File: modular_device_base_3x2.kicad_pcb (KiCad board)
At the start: 2 copper layers, 83.8 x 40.6 mm, 34 parts, among them P1 PWR_JACK_2.5x5.5, P2 BNC_DOUBLE_RA, P3 HEADER_01X03_SMD_RA, P4 HEADER_01X02_SMD_RA, P5 HEADER_01X03_SMD_RA, P6 HEADER_01X02_SMD_RA, SW1 KT_SWITCH, U1 MAX6817

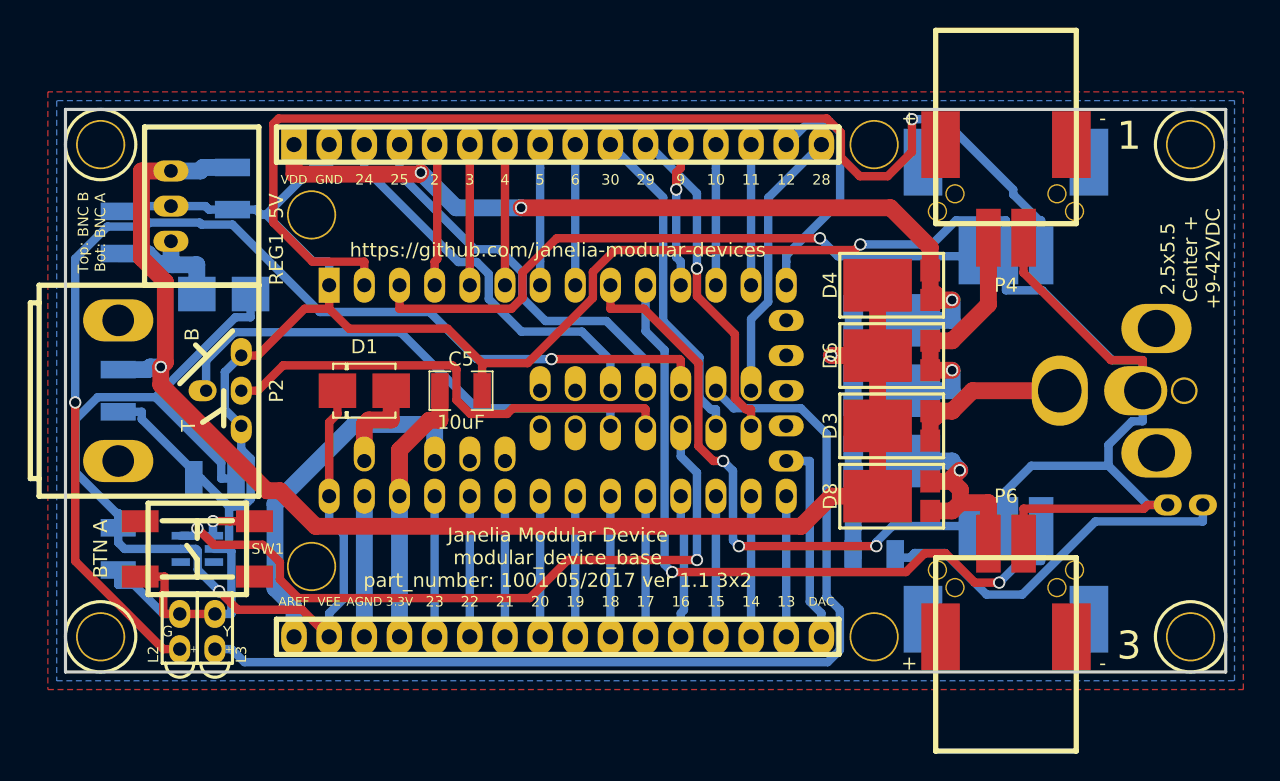
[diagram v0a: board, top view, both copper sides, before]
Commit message: Expanded board.
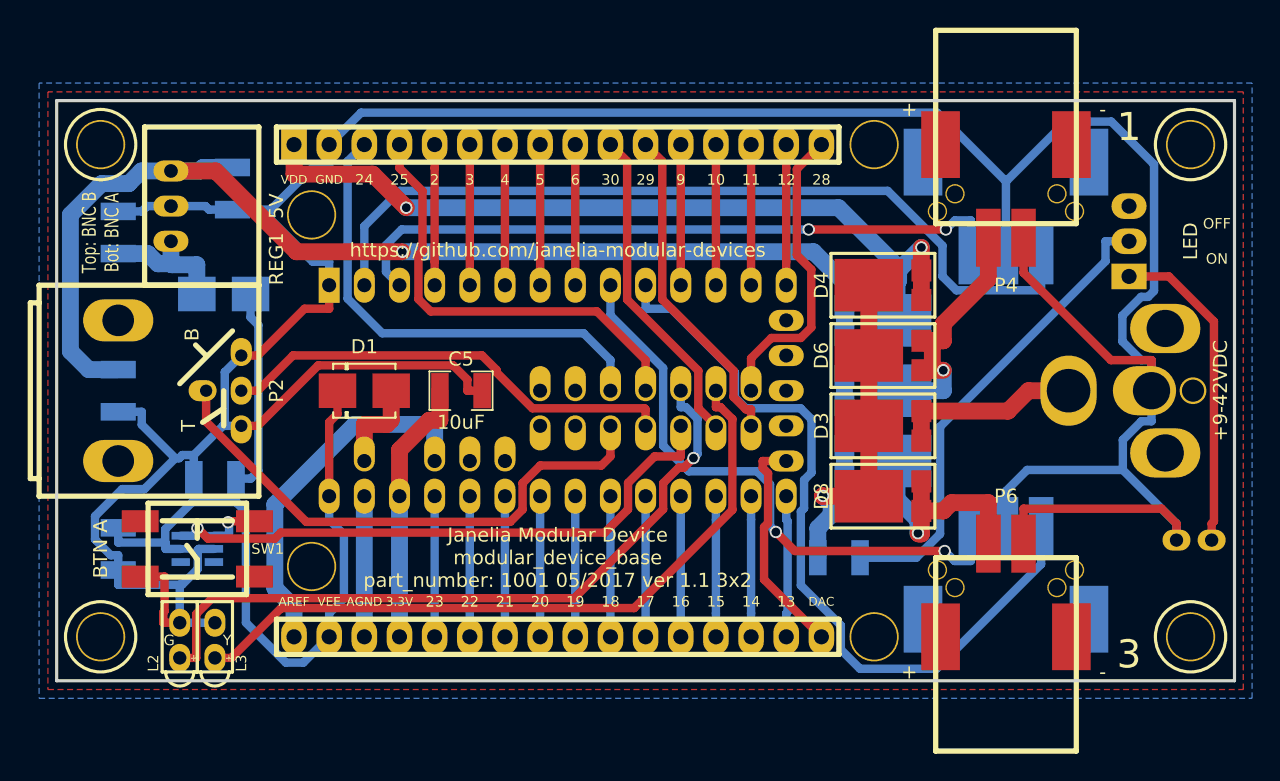
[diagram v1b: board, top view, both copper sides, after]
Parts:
- added P7: HEADER_01X03_RA, footprints:Header_3_Pin_RA, B.Cu at (136.5, 88.9)
- moved L1 2.62 mm to (141.0, 110.5)
- moved R1 2.54 mm to (115.6, 111.8)
- moved P1 0.64 mm to (144.1, 99.7)
- moved D3 0.63 mm to (118.7, 102.2)
- moved D4 0.63 mm to (118.7, 92.1)
- moved D5 0.63 mm to (118.7, 94.6)
- moved D6 0.63 mm to (118.7, 97.2)
- moved D7 0.63 mm to (118.7, 99.7)
- moved D8 0.63 mm to (118.7, 107.3)
- moved D9 0.63 mm to (118.7, 104.8)
- moved L2 0.63 mm to (67.9, 117.5)
- moved L3 0.63 mm to (70.5, 117.5)
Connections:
- R1 pad 2: Net-(L1-Pad1) -> Net-(P7-Pad2)
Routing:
- net GND: track 214.9 -> 256.2 mm, vias 1 -> 0
- net Net-(P7-Pad2): track 0.00 -> 34.3 mm
- net /LED_GRN: track 83.2 -> 51.8 mm, vias 2 -> 1
- net /RX1: track 83.8 -> 61.0 mm, vias 1 -> 0
- net /LED_YEL: track 71.2 -> 51.1 mm
- net /BTN_A_D: track 51.9 -> 42.7 mm, vias 2 -> 1
- net VEE: track 74.3 -> 65.4 mm, vias 1 -> 0
- net /D12: track 17.6 -> 10.2 mm
- net /D24: track 28.5 -> 34.7 mm
- net /TX3: track 52.8 -> 57.1 mm, vias 2 -> 0
- net /BNC_A: track 35.7 -> 39.7 mm
- net /D25: track 28.8 -> 32.4 mm
- net Net-(L1-Pad1): track 27.0 -> 23.3 mm
- net VDD: track 61.1 -> 58.5 mm, vias 3 -> 2
- net /D28: track 19.9 -> 22.0 mm
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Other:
- board size 83.8 x 40.6 mm -> 85.1 x 41.9 mm
- board text added: "+9-42VDC"
- board text added: "LED"
- board text added: "OFF"
- board text added: "ON"
